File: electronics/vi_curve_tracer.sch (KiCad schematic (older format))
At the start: 54 parts, among them P1 CONN_01X05, P2 USB_OTG, P3 CONN_01X03, P4 CONN_01X03, U1 MCP6004, U2 pic24f08km202, U3 ft230x

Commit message: Changed part to the industrial temp range
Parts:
- U1: MPN MCP6L04T-E/ST -> MCP6L04T-I/ST
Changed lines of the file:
@@
 F 2 "SMD_Packages:SSOP-14" H 5450 4800 50  0001 C CNN
 F 3 "" H 5550 4900 50  0000 C CNN
-F 4 "MCP6L04T-E/ST" H 5500 4700 60  0001 C CNN "MPN"
+F 4 "MCP6L04T-I/ST" H 5500 4700 60  0001 C CNN "MPN"
 	1    5500 4700
 	1    0    0    -1
@@
 F 2 "SMD_Packages:SSOP-14" H 7200 3400 50  0001 C CNN
 F 3 "" H 7300 3500 50  0000 C CNN
-F 4 "MCP6L04T-E/ST" H 7250 3300 60  0001 C CNN "MPN"
+F 4 "MCP6L04T-I/ST" H 7250 3300 60  0001 C CNN "MPN"
 	3    7250 3300
 	1    0    0    -1
@@
 F 2 "SMD_Packages:SSOP-14" H 9550 5100 50  0001 C CNN
 F 3 "" H 9650 5200 50  0000 C CNN
-F 4 "MCP6L04T-E/ST" H 9600 5000 60  0001 C CNN "MPN"
+F 4 "MCP6L04T-I/ST" H 9600 5000 60  0001 C CNN "MPN"
 	4    9600 5000
 	1    0    0    -1
@@
 F 2 "SMD_Packages:SSOP-14" H 4250 6300 50  0001 C CNN
 F 3 "" H 4350 6400 50  0000 C CNN
-F 4 "MCP6L04T-E/ST" H 4300 6200 60  0001 C CNN "MPN"
+F 4 "MCP6L04T-I/ST" H 4300 6200 60  0001 C CNN "MPN"
 	2    4300 6200
 	-1   0    0    -1

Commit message: #4 Port complete for C code, had to move DAC outputs to opamp outputs on board to improve impedance
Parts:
- R1: value 1k -> 10k
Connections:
- net DAC_high: now also U2.26 (RB15); no longer U2.25 (RB14)
- net DAC_low: now also U2.7 (RB3); no longer U2.23 (RB12)
- net PWM1: now reaches R7.2, U2.21 (RB10)
- net PWM2: now reaches R6.2, U2.22 (RB11)
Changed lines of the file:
@@
 P 1650 1450
 F 0 "R1" V 1740 1460 50  0000 C CNN
-F 1 "1k" V 1652 1450 50  0000 C CNN
+F 1 "10k" V 1652 1450 50  0000 C CNN
 F 2 "kicad_pcb:SM_0603" V 1580 1450 30  0001 C CNN
 F 3 "" H 1650 1450 30  0000 C CNN
@@
 	6850 3900 7650 3900
 Wire Wire Line
-	3000 3800 6300 3800
-Wire Wire Line
-	3000 3600 5000 3600
-Wire Wire Line
 	7950 2400 7950 3200
 Wire Wire Line
@@
 Connection ~ 7650 3300
 Wire Wire Line
-	5000 3600 5000 3200
-Wire Wire Line
-	5000 3200 5150 3200
+	4500 3200 5150 3200
 Wire Wire Line
 	5750 3200 5750 3300
@@
 	4850 4700 4850 4600
 Connection ~ 4850 4600
-Wire Wire Line
-	6300 3800 6300 4900
 Wire Wire Line
 	9100 5000 9100 4900
@@
 $EndComp
 Wire Wire Line
-	6300 4900 7800 4900
-Wire Wire Line
 	8300 4900 8500 4900
 Wire Wire Line
@@
 	0    1    1    0
 $EndComp
-Text Label 4500 3800 0    60   ~ 0
+Text Label 6750 5500 0    60   ~ 0
 DAC_low
-Text Label 4500 3600 0    60   ~ 0
+Text Label 3250 3500 0    60   ~ 0
 DAC_high
 $Comp
@@
 Wire Wire Line
 	850  6950 850  7050
+Text Label 3250 4000 0    60   ~ 0
+PWM1
+Text Label 3250 3900 0    60   ~ 0
+PWM2
+Wire Wire Line
+	3000 3500 4500 3500
+Wire Wire Line
+	4500 3500 4500 3200
+Wire Wire Line
+	1900 3900 700  3900
+Wire Wire Line
+	700  3900 700  4950
+Wire Wire Line
+	700  4950 3300 4950
+Wire Wire Line
+	3300 4950 3300 5500
+Wire Wire Line
+	3300 5500 7200 5500
+Wire Wire Line
+	7200 5500 7200 4900
+Wire Wire Line
+	7200 4900 7800 4900
 $EndSCHEMATC

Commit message: Changed filter resistors to 3.3k
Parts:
- R11, R13, R14, R8: value 1k -> 3.3k
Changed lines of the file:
@@
 P 5400 3200
 F 0 "R8" V 5490 3210 50  0000 C CNN
-F 1 "1k" V 5402 3200 50  0000 C CNN
+F 1 "3.3k" V 5402 3200 50  0000 C CNN
 F 2 "kicad_pcb:SM_0603" V 5330 3200 30  0001 C CNN
 F 3 "" H 5400 3200 30  0000 C CNN
@@
 P 8750 4900
 F 0 "R11" V 8840 4910 50  0000 C CNN
-F 1 "1k" V 8752 4900 50  0000 C CNN
+F 1 "3.3k" V 8752 4900 50  0000 C CNN
 F 2 "kicad_pcb:SM_0603" V 8680 4900 30  0001 C CNN
 F 3 "" H 8750 4900 30  0000 C CNN
@@
 P 6100 3200
 F 0 "R13" V 6190 3210 50  0000 C CNN
-F 1 "1k" V 6102 3200 50  0000 C CNN
+F 1 "3.3k" V 6102 3200 50  0000 C CNN
 F 2 "kicad_pcb:SM_0603" V 6030 3200 30  0001 C CNN
 F 3 "" H 6100 3200 30  0000 C CNN
@@
 P 8050 4900
 F 0 "R14" V 8140 4910 50  0000 C CNN
-F 1 "1k" V 8052 4900 50  0000 C CNN
+F 1 "3.3k" V 8052 4900 50  0000 C CNN
 F 2 "kicad_pcb:SM_0603" V 7980 4900 30  0001 C CNN
 F 3 "" H 8050 4900 30  0000 C CNN

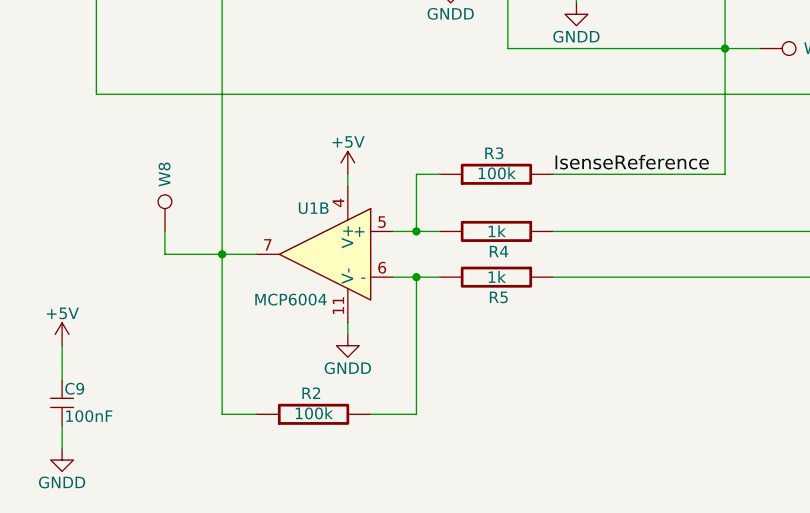
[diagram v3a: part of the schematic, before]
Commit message: Changed vertical scaling from 500uA/div to 5mA/div by reducing opamp gain and by changing the label in the GUI
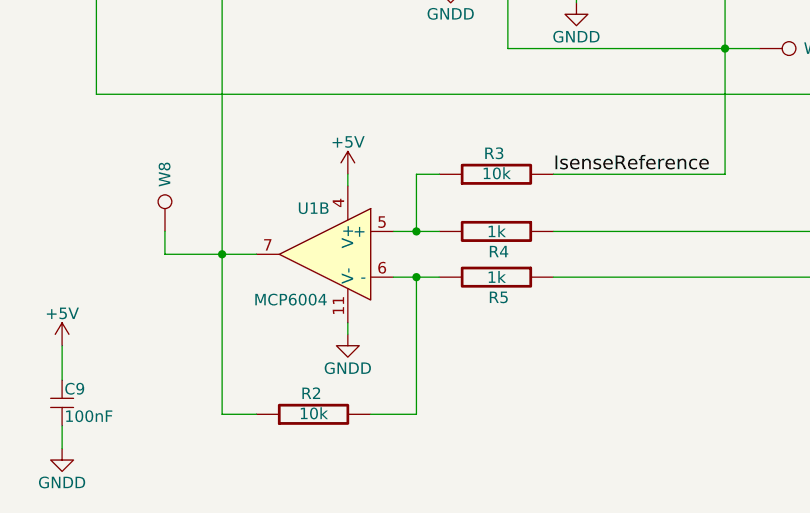
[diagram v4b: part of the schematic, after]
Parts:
- R2, R3: value 100k -> 10k
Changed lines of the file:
@@
 P 5050 5850
 F 0 "R3" V 5140 5860 50  0000 C CNN
-F 1 "100k" V 5052 5850 50  0000 C CNN
+F 1 "10k" V 5052 5850 50  0000 C CNN
 F 2 "kicad_pcb:SM_0603" V 4980 5850 30  0001 C CNN
 F 3 "" H 5050 5850 30  0000 C CNN
@@
 P 4250 6900
 F 0 "R2" V 4340 6910 50  0000 C CNN
-F 1 "100k" V 4252 6900 50  0000 C CNN
+F 1 "10k" V 4252 6900 50  0000 C CNN
 F 2 "kicad_pcb:SM_0603" V 4180 6900 30  0001 C CNN
 F 3 "" H 4250 6900 30  0000 C CNN

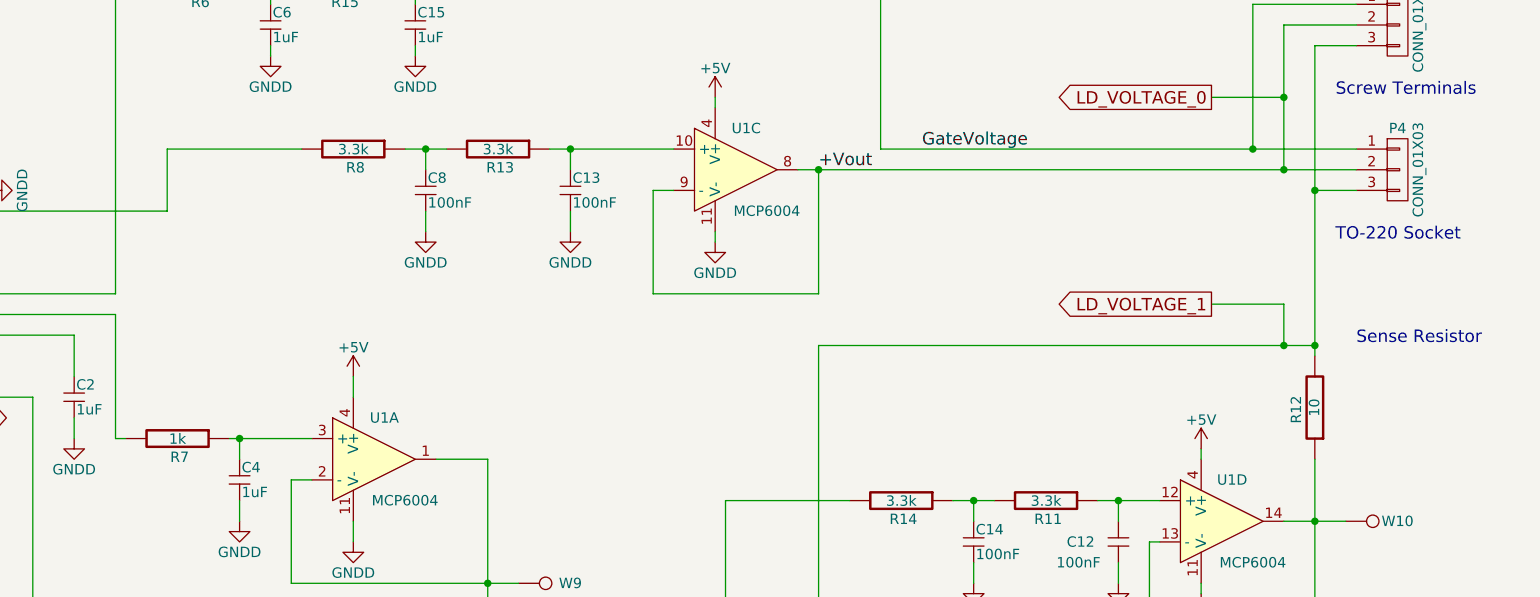
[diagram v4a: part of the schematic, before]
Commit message: Changed R7 to increase filter effectiveness
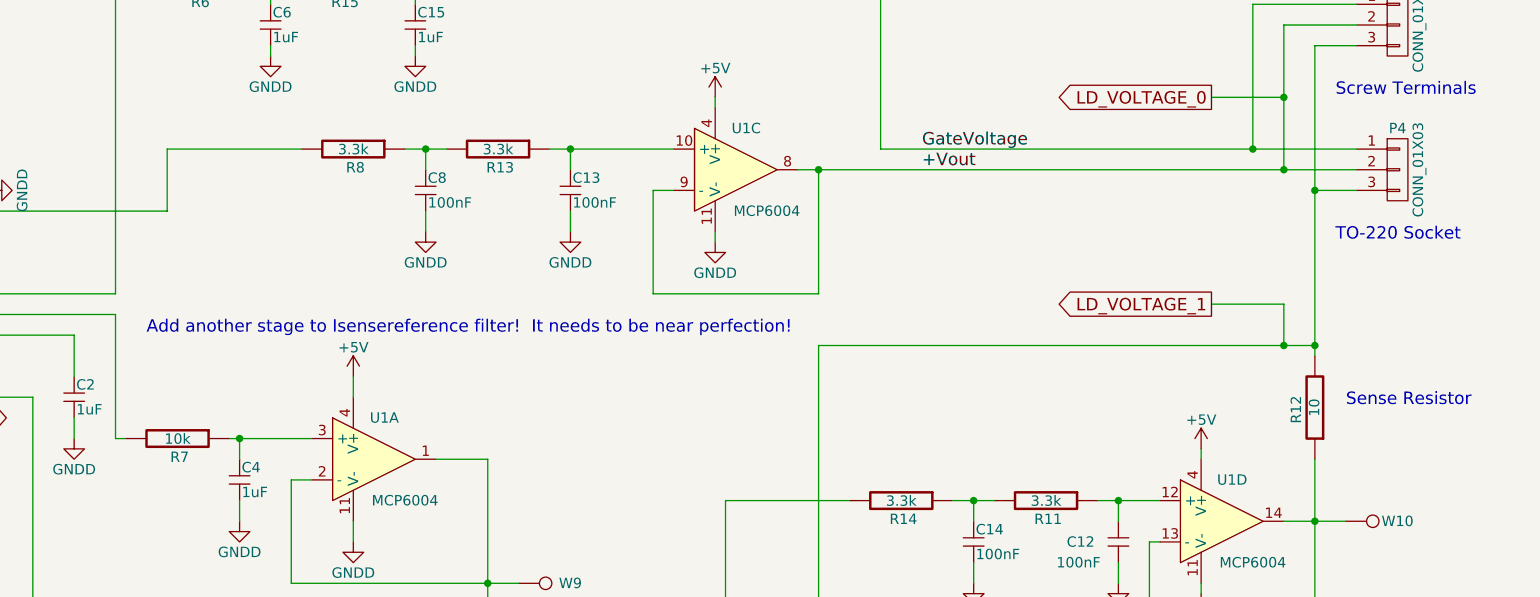
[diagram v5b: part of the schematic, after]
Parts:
- R7: value 1k -> 10k
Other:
- note added: "Add another stage to Isensereference filter! It needs to be near perfection!"
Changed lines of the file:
@@
 P 4550 4600
 F 0 "R7" V 4640 4610 50  0000 C CNN
-F 1 "1k" V 4552 4600 50  0000 C CNN
+F 1 "10k" V 4552 4600 50  0000 C CNN
 F 2 "kicad_pcb:SM_0603" V 4480 4600 30  0001 C CNN
 F 3 "" H 4550 4600 30  0000 C CNN
@@
 	0    -1   -1   0
 $EndComp
-Text Notes 10250 4150 0    60   ~ 0
+Text Notes 10200 4450 0    60   ~ 0
 Sense Resistor
 $Comp
@@
 Wire Wire Line
 	9100 5200 9100 5300
-Text Label 7650 3300 0    60   ~ 0
+Text Label 8150 3300 0    60   ~ 0
 +Vout
 Wire Wire Line
@@
 Wire Wire Line
 	7200 4900 7800 4900
+Text Notes 4400 4100 0    60   ~ 0
+Add another stage to Isensereference filter!  It needs to be near perfection!
 $EndSCHEMATC

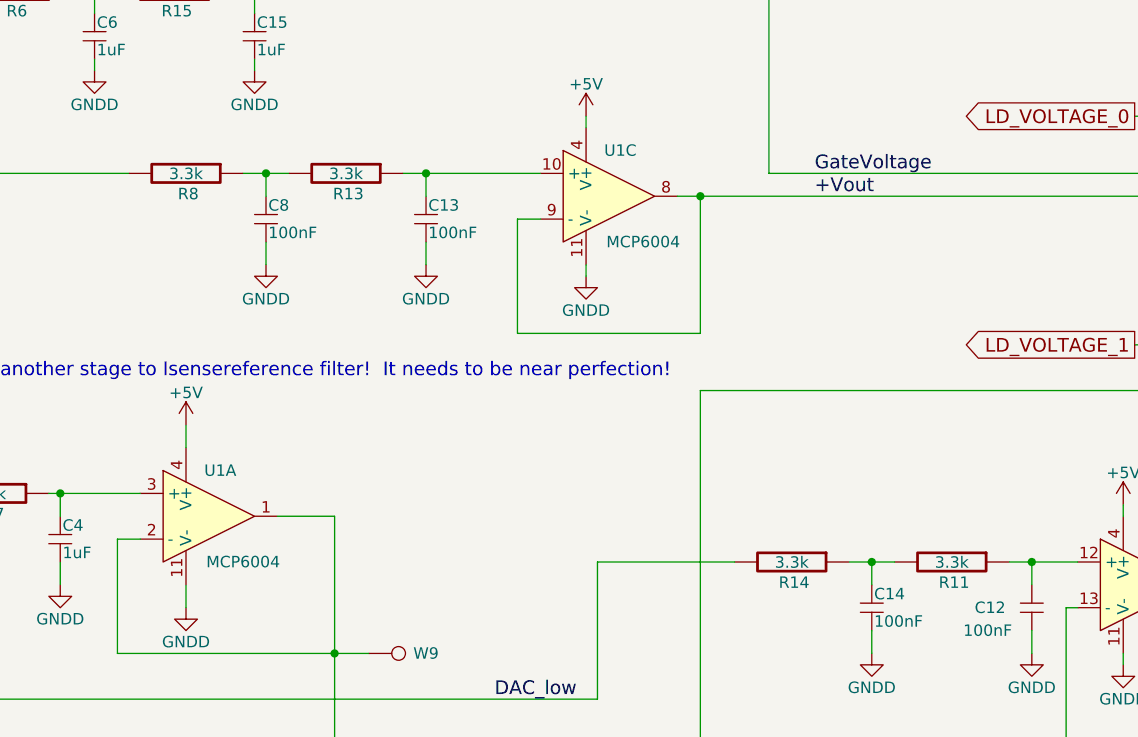
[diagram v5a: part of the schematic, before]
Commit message: Increased the output filter frequency cutoff
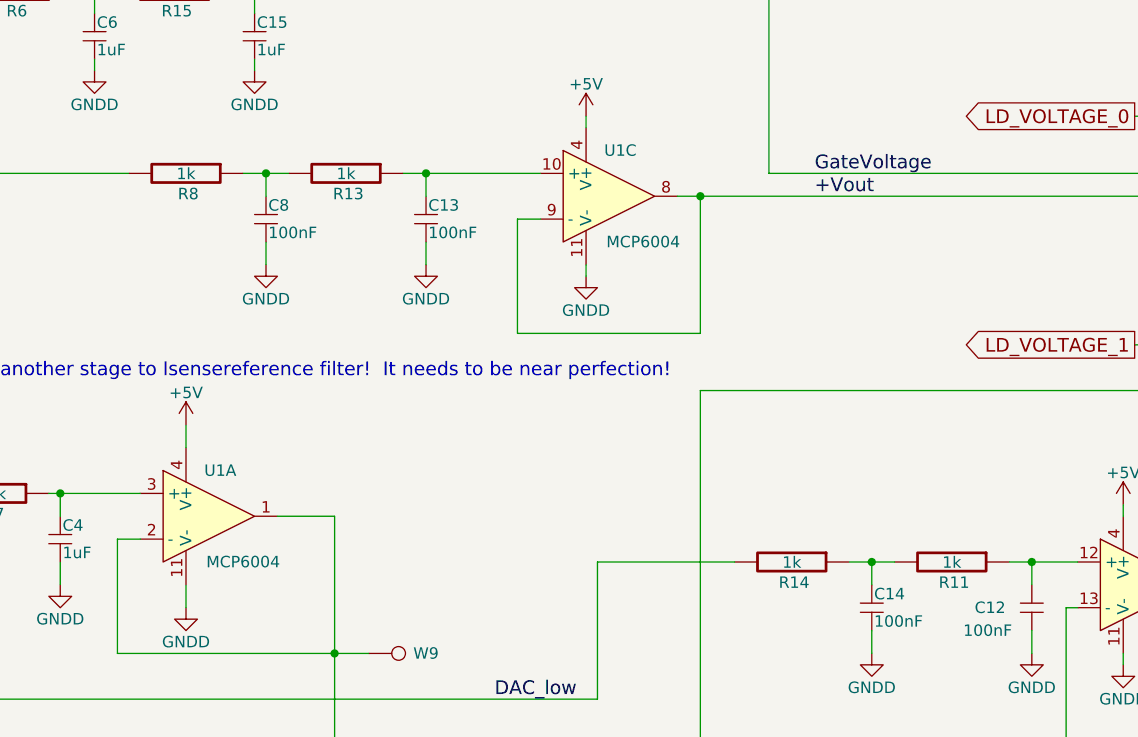
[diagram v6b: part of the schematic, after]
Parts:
- R11, R13, R14, R8: value 3.3k -> 1k
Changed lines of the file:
@@
 P 5400 3200
 F 0 "R8" V 5490 3210 50  0000 C CNN
-F 1 "3.3k" V 5402 3200 50  0000 C CNN
+F 1 "1k" V 5402 3200 50  0000 C CNN
 F 2 "kicad_pcb:SM_0603" V 5330 3200 30  0001 C CNN
 F 3 "" H 5400 3200 30  0000 C CNN
@@
 P 8750 4900
 F 0 "R11" V 8840 4910 50  0000 C CNN
-F 1 "3.3k" V 8752 4900 50  0000 C CNN
+F 1 "1k" V 8752 4900 50  0000 C CNN
 F 2 "kicad_pcb:SM_0603" V 8680 4900 30  0001 C CNN
 F 3 "" H 8750 4900 30  0000 C CNN
@@
 P 6100 3200
 F 0 "R13" V 6190 3210 50  0000 C CNN
-F 1 "3.3k" V 6102 3200 50  0000 C CNN
+F 1 "1k" V 6102 3200 50  0000 C CNN
 F 2 "kicad_pcb:SM_0603" V 6030 3200 30  0001 C CNN
 F 3 "" H 6100 3200 30  0000 C CNN
@@
 P 8050 4900
 F 0 "R14" V 8140 4910 50  0000 C CNN
-F 1 "3.3k" V 8052 4900 50  0000 C CNN
+F 1 "1k" V 8052 4900 50  0000 C CNN
 F 2 "kicad_pcb:SM_0603" V 7980 4900 30  0001 C CNN
 F 3 "" H 8050 4900 30  0000 C CNN

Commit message: Minor rev of electronics, added BOM
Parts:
- added C23: 1uF, kicad_pcb:SM_0603, symbol Csmall
- added R16: 10k, kicad_pcb:SM_0603, symbol R
- C1, C10, C11, C12, C13, C14, C7, C8, C9: Description (none) -> capacitor, 100nF, 0603; MPN (none) -> CC0603ZRY5V7BB104; Manufacturer (none) -> Yageo
- C15, C16, C17, C18, C19, C2, C20, C21, C22, C4, C6: Description (none) -> capacitor, 1uF, 0603; MPN (none) -> CC0603ZRY5V7BB105; Manufacturer (none) -> Yageo
- C3, C5: Description (none) -> capacitor, 47pF, 0603; MPN (none) -> C0603C470J3GACTU; Manufacturer (none) -> Kemet
- P1: Description (none) -> programming header
- P2: Description (none) -> Conn USB Micro-B; MPN (none) -> DX4R005JJ2R1800; Manufacturer (none) -> JAE Electronics; PN DX4R005JJ2R1800 -> (none)
- P3: Description (none) -> terminal block, 5.08mm, 3pos; MPN (none) -> OSTTC032162; Manufacturer (none) -> On Shore Technology, Inc.
- P4: Description (none) -> DIP socket; MPN (none) -> A06-LC-TT; Manufacturer (none) -> Assmann WSW Components; PN A06-LC-TT -> (none)
- R1, R2, R3, R7: Description (none) -> resistor, 10kohm, 0603; MPN (none) -> RC0603FR-0710KL; Manufacturer (none) -> Yageo
- R10, R9: Description (none) -> resistor, 27ohm, 0603; MPN (none) -> RC0603FR-0727RL; Manufacturer (none) -> Yageo
- R11, R13, R14, R15, R4, R5, R6, R8: Description (none) -> resistor, 1kohm, 0603; MPN (none) -> RC0603FR-071KL; Manufacturer (none) -> Yageo
- R12: Description (none) -> resistor, 10ohm, 0603; MPN (none) -> RC0603FR-0710RL; Manufacturer (none) -> Yageo
- U1: Description (none) -> Opamp 1MHz, Quad, TSSOP-14; Manufacturer (none) -> Microchip
- U2: Description (none) -> Microcontroller; MPN (none) -> PIC24FV16KM202; Manufacturer (none) -> Microchip, Inc.
- U3: Description (none) -> USB-to-UART, IC, SSOP-16; MPN (none) -> FT230XS-R; Manufacturer (none) -> FTDI
- W1, W10, W2, W3, W4, W5, W6, W7, W8, W9: Description (none) -> test point
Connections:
- net GNDD: now also C23.2
- net PWM1: now also R16.2; no longer R7.2
- new net: C23.1, R16.1, R7.2
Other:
- note removed: "Add another stage to Isensereference filter! It needs to be near perfection!"
- moved on the sheet: C1, C16, C17, C18, C19, C20, C21, C22, C4, C9, P1, R1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

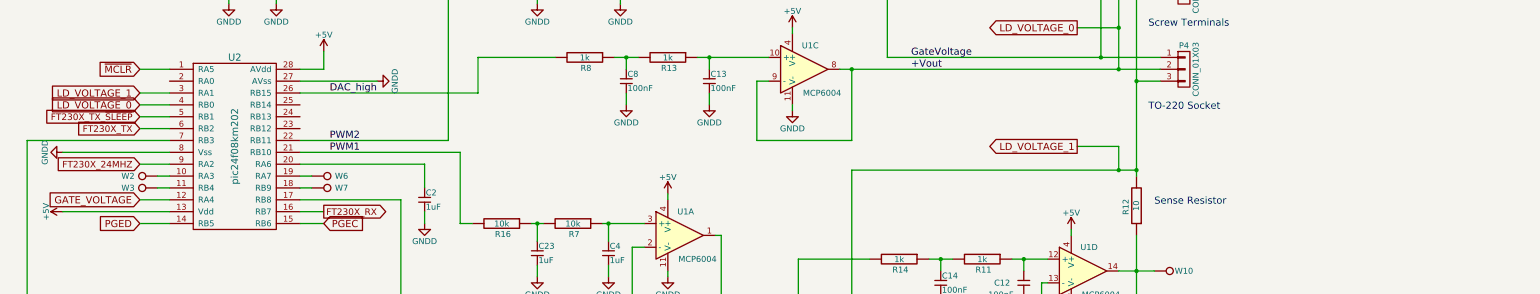
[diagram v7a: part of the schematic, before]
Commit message: See #5 - Added patch wire to control the gate voltage
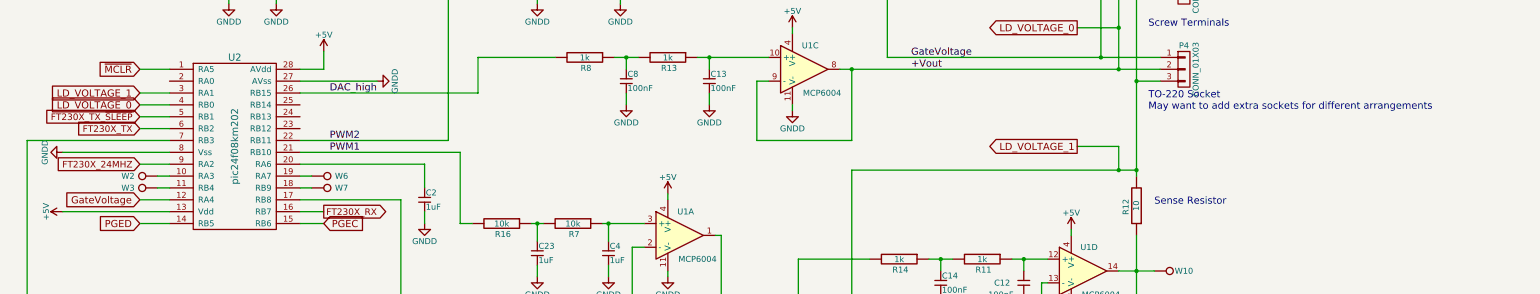
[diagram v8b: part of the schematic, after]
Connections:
- net GATE_VOLTAGE is gone; now on net GateVoltage: U2.12 (RA4)
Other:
- note added: "TO-220 Socket\nMay want to add extra sockets for different arrangements"
- note removed: "TO-220 Socket"
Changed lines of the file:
@@
 $EndComp
 Text GLabel 1650 4400 0    60   Input ~ 0
-GATE_VOLTAGE
+GateVoltage
 $Comp
 L R R9
@@
 $EndComp
 Text Notes 10150 3650 0    60   ~ 0
-TO-220 Socket
+TO-220 Socket\nMay want to add extra sockets for different arrangements
 Text Notes 10150 2950 0    60   ~ 0
 Screw Terminals
